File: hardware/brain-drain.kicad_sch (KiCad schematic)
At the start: 0 parts

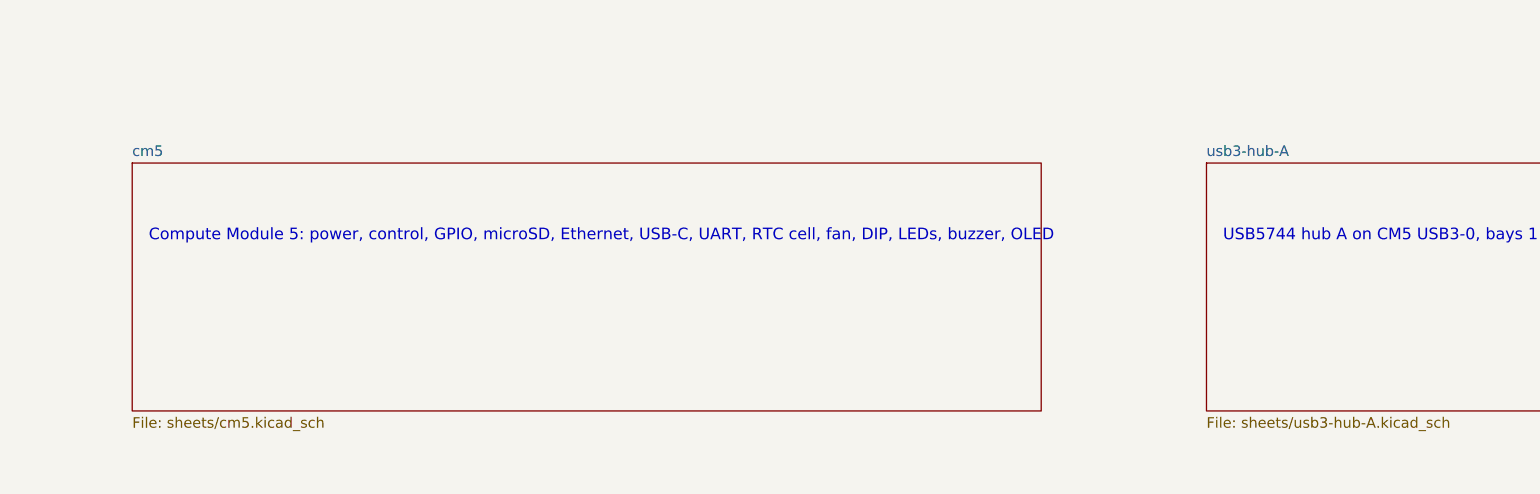
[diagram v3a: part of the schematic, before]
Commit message: design v2: wireless brain box (C22-C23) — no Ethernet, no buzzer, passive cooler, hinged lid, Wi-Fi AP + QR + phone page, fabrication guide
hardware: 136x100 outline, CM5 wireless antenna edge on the left board edge with a copper-free
strip (rule area), DIN/USB-C/microSD on the right wall, M.2 along the front under the lid, lid
microswitch, CR2032 + service headers on the bottom; magjack and buzzer removed from the
netlist; check_place clean, DRC 0 errors; schematic + connections regenerated, render script
also exports the schematic
software: wifi.py (nmcli / simulated backends, ephemeral key, join, resets), webui.py (stdlib
HTTP phone page: status, certificates, log, join, reset), qr.py, OLED frames with the Wi-Fi QR
code, DIP mode 110 = SERVICE, braindrain wifi-reset; 74 tests, ruff clean; qrcode dependency
enclosure: hinged lid (rear knuckles, filament pin, front snap latch), vents on the antenna side
and front, right-wall cutouts, lid-open scene render
docs: C22/C23, FABRICATION.md (vendors, cost estimate, gates), STATUS R19-R20, panels rear/right,
OLED Wi-Fi mockup, README/ARCHITECTURE/USAGE/BOM/CHANGELOG/HISTORY/tracker updated

Co-Authored-By: Claude Fable 5.1 <noreply@anthropic.com>
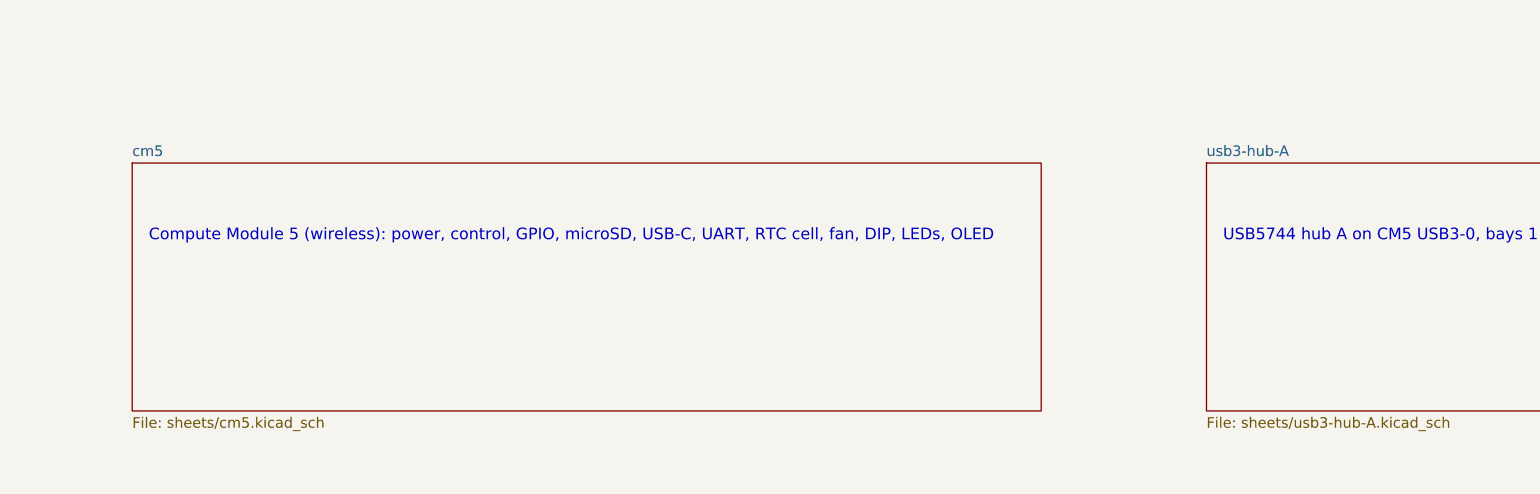
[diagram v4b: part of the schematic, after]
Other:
- note added: "Compute Module 5 (wireless): power, control, GPIO, microSD, USB-C, UART, RTC cell, fan, DIP, LEDs, OLED"
- note removed: "Compute Module 5: power, control, GPIO, microSD, Ethernet, USB-C, UART, RTC cell, fan, DIP, LEDs, buzzer, OLED"
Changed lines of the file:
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@@
 		)
 	)
-	(text "Compute Module 5: power, control, GPIO, microSD, Ethernet, USB-C, UART, RTC cell, fan, DIP, LEDs, buzzer, OLED"
+	(text "Compute Module 5 (wireless): power, control, GPIO, microSD, USB-C, UART, RTC cell, fan, DIP, LEDs, OLED"
 		(exclude_from_sim no)
 		(at 292 33 0)

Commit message: docs: C24 brain + bay cards — decisions, architecture, BOM card table, fabrication, README, USAGE, STATUS, changelog, history; diagrams: 8 slots, lid plan, left wall
Co-Authored-By: Claude Fable 5.1 <noreply@anthropic.com>
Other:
- removed sheet bay-switch-1
- removed sheet bay-switch-2
- removed sheet bay-switch-3
- removed sheet bay-switch-4
- removed sheet bridge-1
- removed sheet bridge-2
- removed sheet bridge-3
- removed sheet bridge-4
- added sheet bay-slots (sheets/bay-slots.kicad_sch)
- note added: "12 V DIN input, fuse, TVS, reverse-polarity FET, bulk capacitance (sized for 8 bays)"
- note added: "Bay 9: M.2 M-key on PCIe Gen3 x1, 3V3_M2 buck + load switch, lid switch"
- note added: "Eight bay slots (PCIe x1 sockets, bay-card pinout): USB 3, USB 2, 12 V, 5 V, BAY_EN, bay LEDs"
- note added: "USB5744 hub A on CM5 USB3-0, bay slots 1-4"
- note added: "USB5744 hub B on CM5 USB3-1, bay slots 5-8"
- note added: "brain-drain brain: CM5, two USB 3 hubs, eight bay slots, M.2 bay, power, UI"
- note removed: "12 V DIN input, fuse, TVS, reverse-polarity FET, bulk capacitance"
- note removed: "Bay 1: ASM1153E USB-SATA bridge and 22-pin SATA receptacle"
- note removed: "Bay 1: switched 12 V and 5 V with soft-start and PTC fuses"
- note removed: "Bay 2: ASM1153E USB-SATA bridge and 22-pin SATA receptacle"
- note removed: "Bay 2: switched 12 V and 5 V with soft-start and PTC fuses"
- note removed: "Bay 3: ASM1153E USB-SATA bridge and 22-pin SATA receptacle"
- note removed: "Bay 3: switched 12 V and 5 V with soft-start and PTC fuses"
- note removed: "Bay 4: ASM1153E USB-SATA bridge and 22-pin SATA receptacle"
- note removed: "Bay 4: switched 12 V and 5 V with soft-start and PTC fuses"
- note removed: "Bay 5: M.2 M-key on PCIe Gen3 x1, 3V3_M2 buck + load switch, door switch"
- note removed: "USB5744 hub A on CM5 USB3-0, bays 1 and 2"
- note removed: "USB5744 hub B on CM5 USB3-1, bays 3 and 4"
- note removed: "brain-drain 4-bay disk sanitizer carrier, CM5"
- title: brain-drain 4-bay disk sanitizer carrier, CM5 -> brain-drain brain: CM5, two USB 3 hubs, eight bay slots, M.2 bay, power, UI
